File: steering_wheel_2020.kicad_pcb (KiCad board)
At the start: 2 copper layers, 38 parts, among them J1 VEHICLE, J10 Conn_01x15, J11 Conn_01x15, J12 ALT_PWR, J2 DEBUG, J3 Conn_01x15, J4 Conn_01x13, J5 Conn_01x15, J6 Conn_01x13, J7 Conn_01x15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

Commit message: begin layout
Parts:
- added REF**: MountingHole_2.2mm_M2, MountingHole:MountingHole_2.2mm_M2, F.Cu at (139.1, 39.4)
- added REF**: MountingHole_2.2mm_M2, MountingHole:MountingHole_2.2mm_M2, F.Cu at (188.6, 39.4)
- added REF**: MountingHole_2.2mm_M2, MountingHole:MountingHole_2.2mm_M2, F.Cu at (188.6, 84.5)
- added REF**: MountingHole_2.2mm_M2, MountingHole:MountingHole_2.2mm_M2, F.Cu at (139.1, 84.5)
- C1, C5, C8, C9, D1, D3, D4, F1: moved to B.Cu
- Y1: footprint Crystal:Crystal_SMD_HC49-SD -> rahulsalvi:Crystal_SMD_TXC_7A-2Pin_5x3.2mm_HandSolder
- moved J9 129.2 mm to (184.0, 44.1)
- moved J10 127.1 mm to (186.6, 44.1)
- moved D4 125.9 mm to (157.5, 45.1), turned to 90 degrees
- moved J11 125.1 mm to (189.1, 44.1)
- moved D3 118.2 mm to (160.7, 45.1), turned to 90 degrees
- moved J4 114.2 mm to (179.1, 79.5), turned to 270 degrees
- moved J6 112.9 mm to (179.1, 82.0), turned to 270 degrees
- moved J8 111.6 mm to (179.1, 84.6), turned to 270 degrees
- moved J3 110.5 mm to (143.4, 79.6), turned to 180 degrees
- moved C6 106.5 mm to (163.8, 73.9)
- moved J5 104.0 mm to (140.8, 79.6), turned to 180 degrees
- moved F1 98.0 mm to (156.5, 50.2)
- moved J7 97.5 mm to (138.3, 79.6), turned to 180 degrees
- moved J2 89.8 mm to (167.6, 45.7)
- moved D1 88.6 mm to (151.1, 57.1), turned to 270 degrees
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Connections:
- J3 pad 1: PC0 -> PC3
- J3 pad 10: PC9 -> PC7
- J3 pad 11: PC10 -> PC8
- J3 pad 12: PC11 -> PC9
- J3 pad 14: PC13 -> PC11
- J3 pad 15: PC14 -> PC10
- J3 pad 2: PC1 -> PC2
- J3 pad 3: PC2 -> PC1
- J3 pad 4: PC3 -> PC0
- J3 pad 7: PC6 -> PC14
- J3 pad 8: PC7 -> PC13
- J3 pad 9: PC8 -> PC6
- J4 pad 1: PA0 -> PA8
- J4 pad 10: PA9 -> PA1
- J4 pad 11: PA10 -> PA0
- J4 pad 2: PA1 -> PA9
- J4 pad 3: PA2 -> PA10
- J4 pad 4: PA3 -> PA7
- J4 pad 5: PA4 -> PA6
- J4 pad 7: PA6 -> PA4
- J4 pad 8: PA7 -> PA3
- J4 pad 9: PA8 -> PA2
- J9 pad 1: PB0 -> PB15
- J9 pad 10: PB10 -> PB9
- J9 pad 12: PB12 -> PB10
- J9 pad 13: PB13 -> PB2
- J9 pad 14: PB14 -> PB1
- J9 pad 15: PB15 -> PB0
- J9 pad 2: PB1 -> PB14
- J9 pad 3: PB2 -> PB13
- J9 pad 4: PB4 -> PB12
- J9 pad 5: PB5 -> PB4
- J9 pad 6: PB6 -> PB5
- J9 pad 7: PB7 -> PB6
- J9 pad 8: PB8 -> PB7
- J9 pad 9: PB9 -> PB8
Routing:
- net Net-(C9-Pad1): track 0.00 -> 14.1 mm, vias 0 -> 1
- net VIN: track 0.00 -> 8.22 mm
- net Net-(C13-Pad1): track 0.00 -> 8.07 mm
- net Net-(C12-Pad1): track 0.00 -> 8.06 mm
- net 5V: track 0.00 -> 7.04 mm
- net 3V3: track 0.00 -> 5.32 mm
- net 12V: track 0.00 -> 4.97 mm
- net GND: track 0.00 -> 2.93 mm, vias 0 -> 1
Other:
- board outline added: 55.9 x 51.4 mm
- net class Default: clearance 0.2 -> 0.1524; trace_width 0.25 -> 0.1524; via_dia 0.8 -> 0.6096; via_drill 0.4 -> 0.3048
- net class Power added: clearance 0.1524, trace_width 1.524, via_dia 3.048, via_drill 1.524
- rule trace_clearance: 0.2 -> 0.1524
- rule trace_min: 0.2 -> 0.1524
- rule via_min_drill: 0.3 -> 0.3048
- rule via_min_size: 0.4 -> 0.6096

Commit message: routing mostly done
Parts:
- C2, C3, C4, C6, C7: moved to B.Cu
- moved R2 77.7 mm to (177.8, 46.4), turned to 270 degrees
- moved R1 66.5 mm to (172.0, 46.4), turned to 270 degrees
- moved C10 62.1 mm to (175.0, 46.4), turned to 270 degrees
- moved C2 34.8 mm to (162.4, 66.0), turned to 45 degrees
- moved C6 6.48 mm to (163.8, 67.4), turned to 45 degrees
- moved C3 6.39 mm to (164.2, 61.5)
- moved C7 4.93 mm to (172.5, 69.6), turned to 225 degrees
- moved J1 3.17 mm to (165.1, 38.7)
- moved J2 3.17 mm to (167.6, 42.5)
- moved JP1 3.17 mm to (172.7, 42.5)
- moved C4 3.12 mm to (164.3, 75.3), turned to 270 degrees
- moved C5 2.29 mm to (161.0, 64.6), turned to 45 degrees
- moved U2 2.05 mm to (175.9, 52.8)
- moved C1 1.99 mm to (155.1, 63.9)
- moved D2 1.81 mm to (164.0, 53.3), turned to 90 degrees
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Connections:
- J2 pad 5: SWO -> NRST
- J2 pad 6: NRST -> SWO
- J3 pad 1: PC3 -> PC1
- J3 pad 10: PC7 -> PB5
- J3 pad 11: PC8 -> PB4
- J3 pad 12: PC9 -> PC12
- J3 pad 13: PC12 -> PC11
- J3 pad 14: PC11 -> PC10
- J3 pad 15: PC10 -> PA15
- J3 pad 2: PC2 -> PC0
- J3 pad 3: PC1 -> PC15
- J3 pad 4: PC0 -> PC14
- J3 pad 5: PC4 -> PC13
- J3 pad 6: PC5 -> PB9
- J3 pad 7: PC14 -> PB8
- J3 pad 8: PC13 -> PB7
- J3 pad 9: PC6 -> PB6
- J4 pad 1: PA8 -> PB0
- J4 pad 12: PA15 -> PC3
- J4 pad 13: PC15 -> PC2
- J4 pad 2: PA9 -> PC5
- J4 pad 3: PA10 -> PC4
- J9 pad 1: PB15 -> PA10
- J9 pad 10: PB9 -> PB13
- J9 pad 11: PB11 -> PB12
- J9 pad 12: PB10 -> PB11
- J9 pad 13: PB2 -> PB10
- J9 pad 14: PB1 -> PB2
- J9 pad 15: PB0 -> PB1
- J9 pad 2: PB14 -> PA9
- J9 pad 3: PB13 -> PA8
- J9 pad 4: PB12 -> PC9
- J9 pad 5: PB4 -> PC8
- J9 pad 6: PB5 -> PC7
- J9 pad 7: PB6 -> PC6
- J9 pad 8: PB7 -> PB15
- J9 pad 9: PB8 -> PB14
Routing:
- net (no net): track 0.00 -> 70.2 mm, vias 0 -> 13
- net 3V3: track 5.32 -> 40.0 mm, vias 0 -> 9
- net PC1: track 0.00 -> 31.9 mm, vias 0 -> 1
- net PA10: track 0.00 -> 29.3 mm
- net GND: track 2.93 -> 32.1 mm, vias 1 -> 12
- net PC0: track 0.00 -> 28.4 mm, vias 0 -> 1
- net PA15: track 0.00 -> 27.3 mm, vias 0 -> 1
- net PA9: track 0.00 -> 26.8 mm
- net PC10: track 0.00 -> 24.9 mm, vias 0 -> 1
- net PA8: track 0.00 -> 24.5 mm
- net NRST: track 0.00 -> 24.4 mm, vias 0 -> 2
- net PB1: track 0.00 -> 23.2 mm
- net PC11: track 0.00 -> 22.3 mm, vias 0 -> 1
- net PB4: track 0.00 -> 22.0 mm
- net PC9: track 0.00 -> 21.8 mm
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- added copper zone on F.Cu, net 3V3
- added copper zone on B.Cu, net GND

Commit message: clean up some traces
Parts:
- moved C1 2.99 mm to (152.1, 63.2), turned to 180 degrees
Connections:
- J12 pad 3: (no net) -> GND
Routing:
- net 3V3: track 40.0 -> 55.6 mm
- net GND: track 32.1 -> 25.5 mm
- net PC15: track 20.7 -> 19.7 mm
- net PC0: track 28.4 -> 27.6 mm

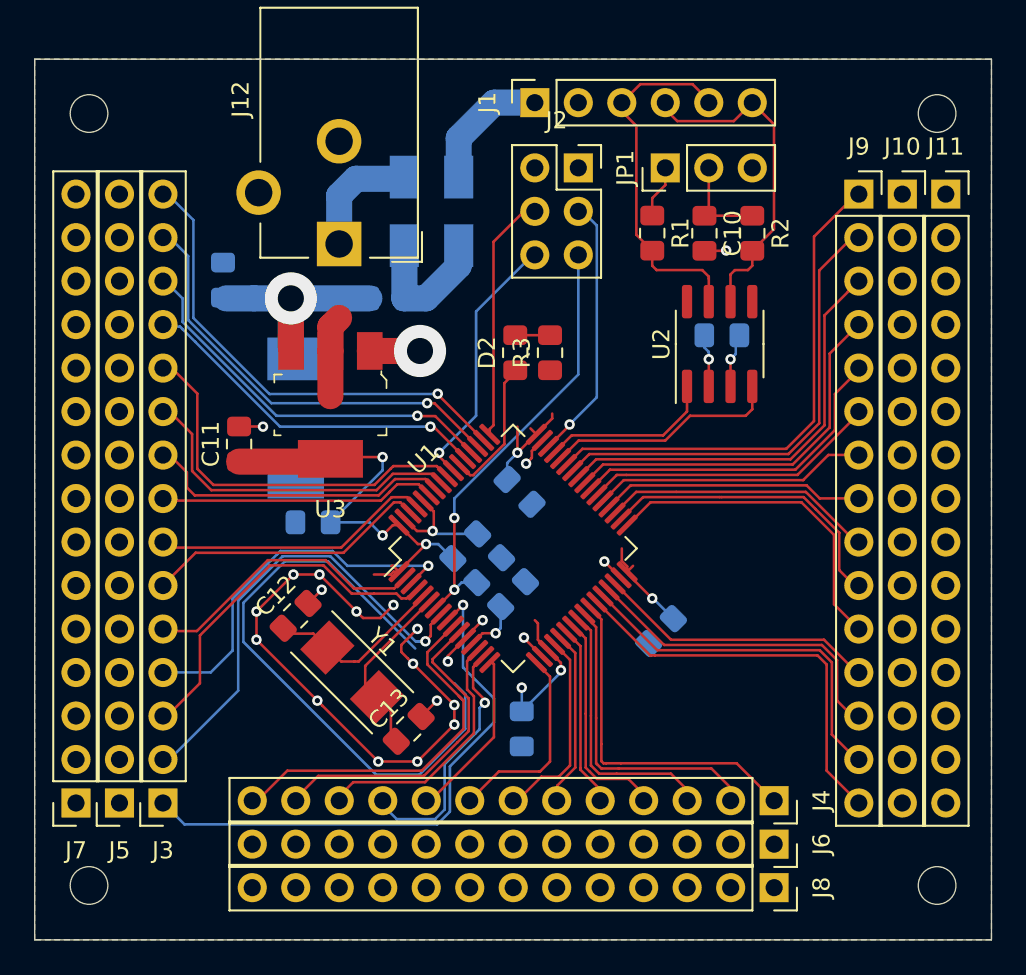
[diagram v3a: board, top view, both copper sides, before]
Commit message: silkscreen done
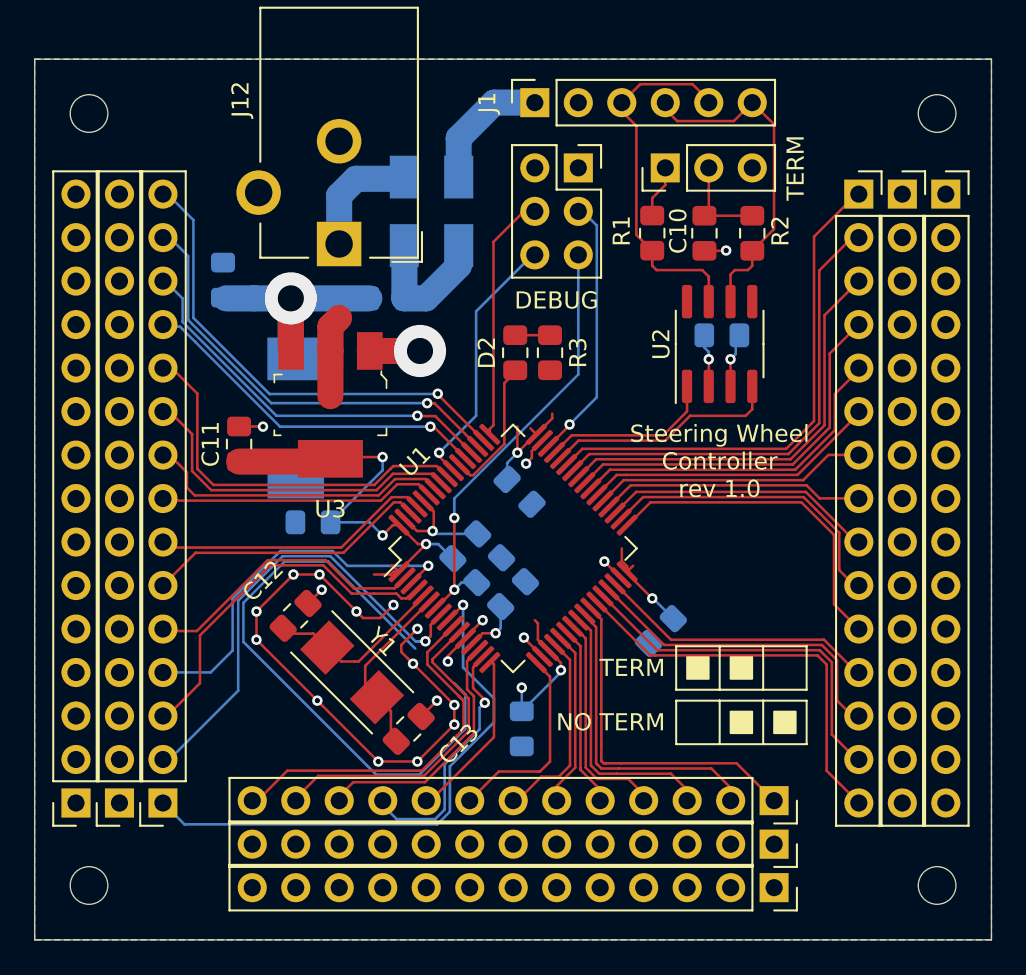
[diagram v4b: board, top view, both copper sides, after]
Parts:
- renumbered J2 to DEBUG, JP1 to TERM
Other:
- board text added: "+"
- board text added: "-"
- board text added: "H"
- board text added: "L"
- board text added: "NO TERM"
- board text added: "S"
- board text added: "Steering Wheel Controller rev 1.0"
- board text added: "TERM"

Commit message: solder mask clearance
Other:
- rule pad_to_mask_clearance: 0.051 -> 0.05
- rule solder_mask_min_width: 0.25 -> 0.1
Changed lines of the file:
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@@
     (pad_size 1.524 1.524)
     (pad_drill 0.762)
-    (pad_to_mask_clearance 0.051)
-    (solder_mask_min_width 0.25)
+    (pad_to_mask_clearance 0.05)
+    (solder_mask_min_width 0.1)
     (aux_axis_origin 0 0)
     (visible_elements FFFFFF7F)
@@
       (outputformat 1)
       (mirror false)
-      (drillshape 1)
+      (drillshape 0)
       (scaleselection 1)
-      (outputdirectory ""))
+      (outputdirectory "gerber/"))
   )
   (net 0 "")

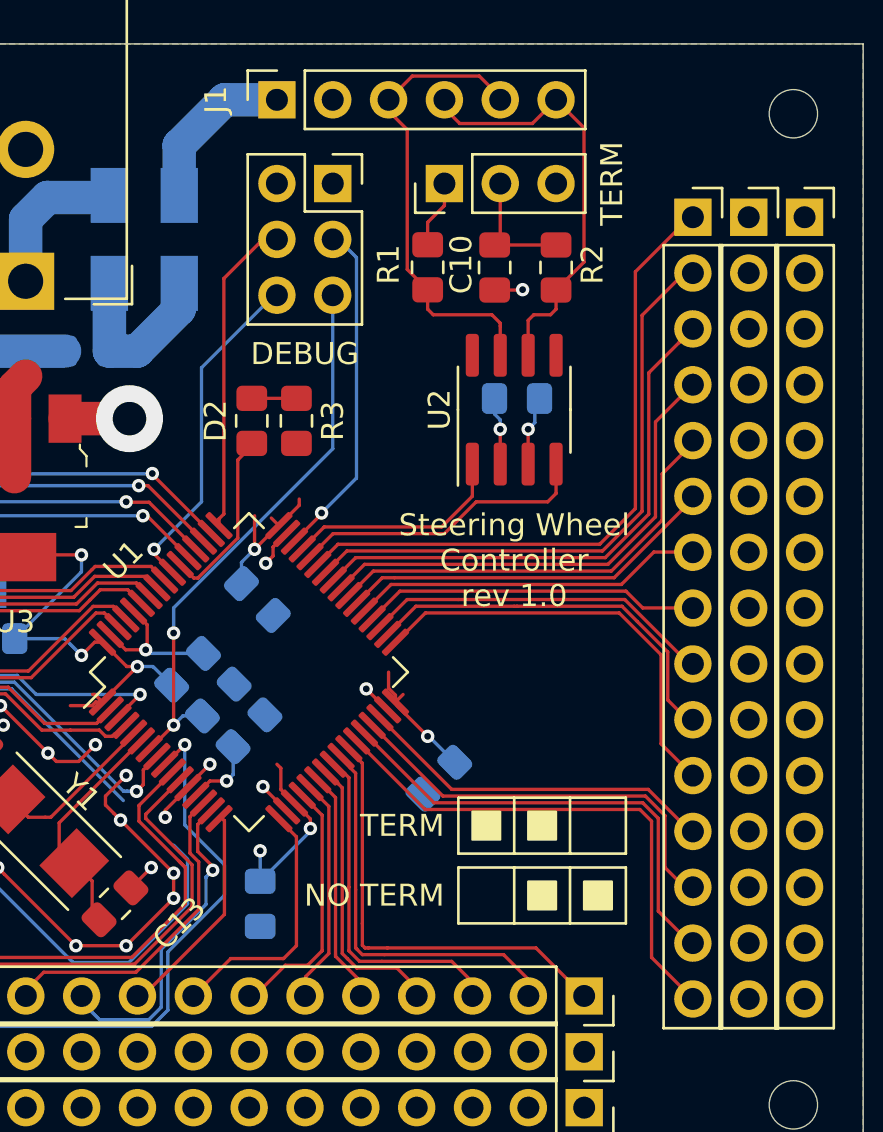
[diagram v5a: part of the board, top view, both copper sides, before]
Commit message: Added headers for BOOT0 and BOOT1
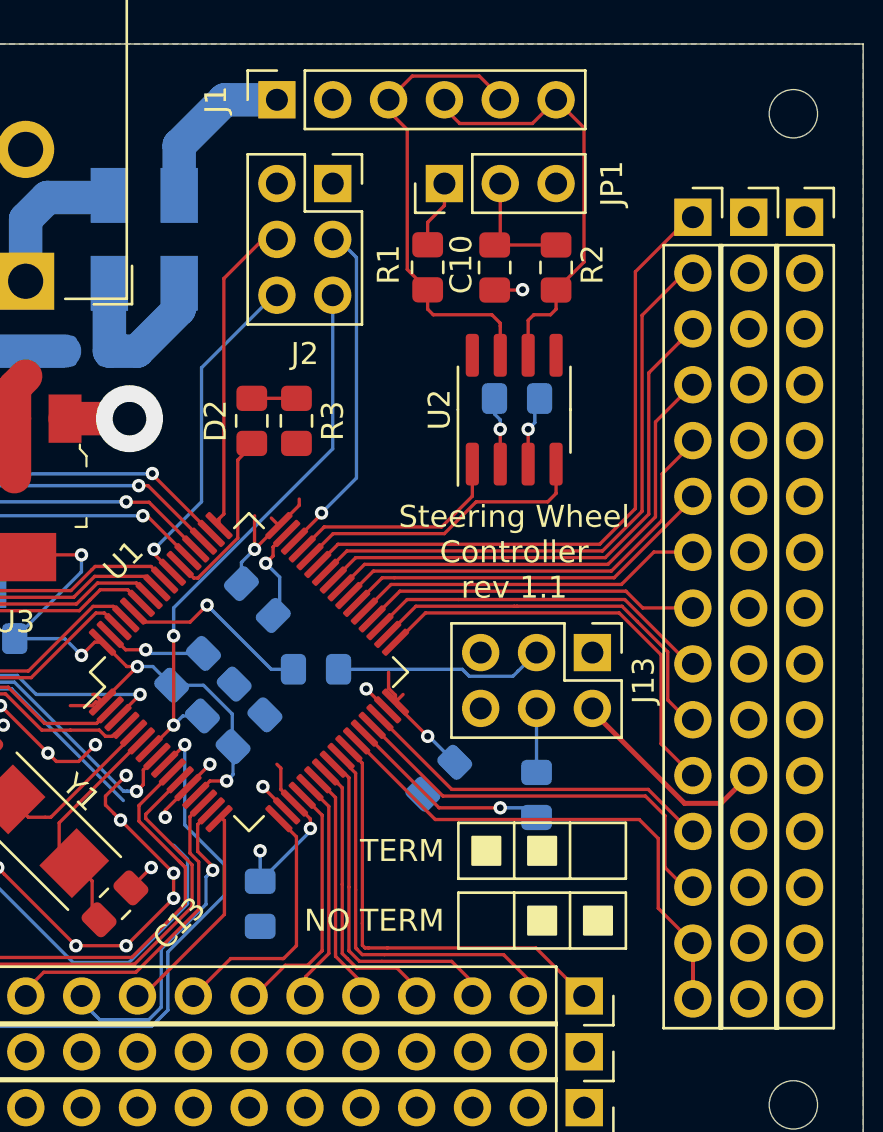
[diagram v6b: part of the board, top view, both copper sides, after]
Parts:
- added J13: BOOT, Connector_PinHeader_2.54mm:PinHeader_2x03_P2.54mm_Vertical, F.Cu at (179.5, 63.9)
- added R4: 10k, Resistor_SMD:R_0805_2012Metric_Pad1.15x1.40mm_HandSolder, B.Cu at (166.9, 64.6)
- added R5: 10k, Resistor_SMD:R_0805_2012Metric_Pad1.15x1.40mm_HandSolder, B.Cu at (176.9, 70.4)
- renumbered DEBUG to J2, TERM to JP1
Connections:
- J9 pad 14: PB2 -> PB1
- U1 pad 28: PB2 -> BOOT1
- U1 pad 60: GND -> BOOT0
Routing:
- net PB2: track 20.7 -> 0.00 mm
- net 3V3: track 55.6 -> 69.7 mm
- net Net-(J13-Pad3): track 0.00 -> 9.59 mm
- net BOOT1: track 0.00 -> 9.42 mm, vias 0 -> 1
- net BOOT0: track 0.00 -> 9.02 mm, vias 0 -> 1
- net Net-(J13-Pad4): track 0.00 -> 2.92 mm
- net PB1: track 23.2 -> 26.0 mm
- net GND: track 25.5 -> 26.0 mm
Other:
- board text added: "0"
- board text added: "1"
- board text added: "BOOT"
- board text added: "Steering Wheel Controller rev 1.1"
- board text removed: "Steering Wheel Controller rev 1.0"
